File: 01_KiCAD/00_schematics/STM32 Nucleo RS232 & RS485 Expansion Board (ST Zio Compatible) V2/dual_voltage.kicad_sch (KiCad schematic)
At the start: 23 parts, among them IC1 REG103GA-A, U1 TPS2117DRLR

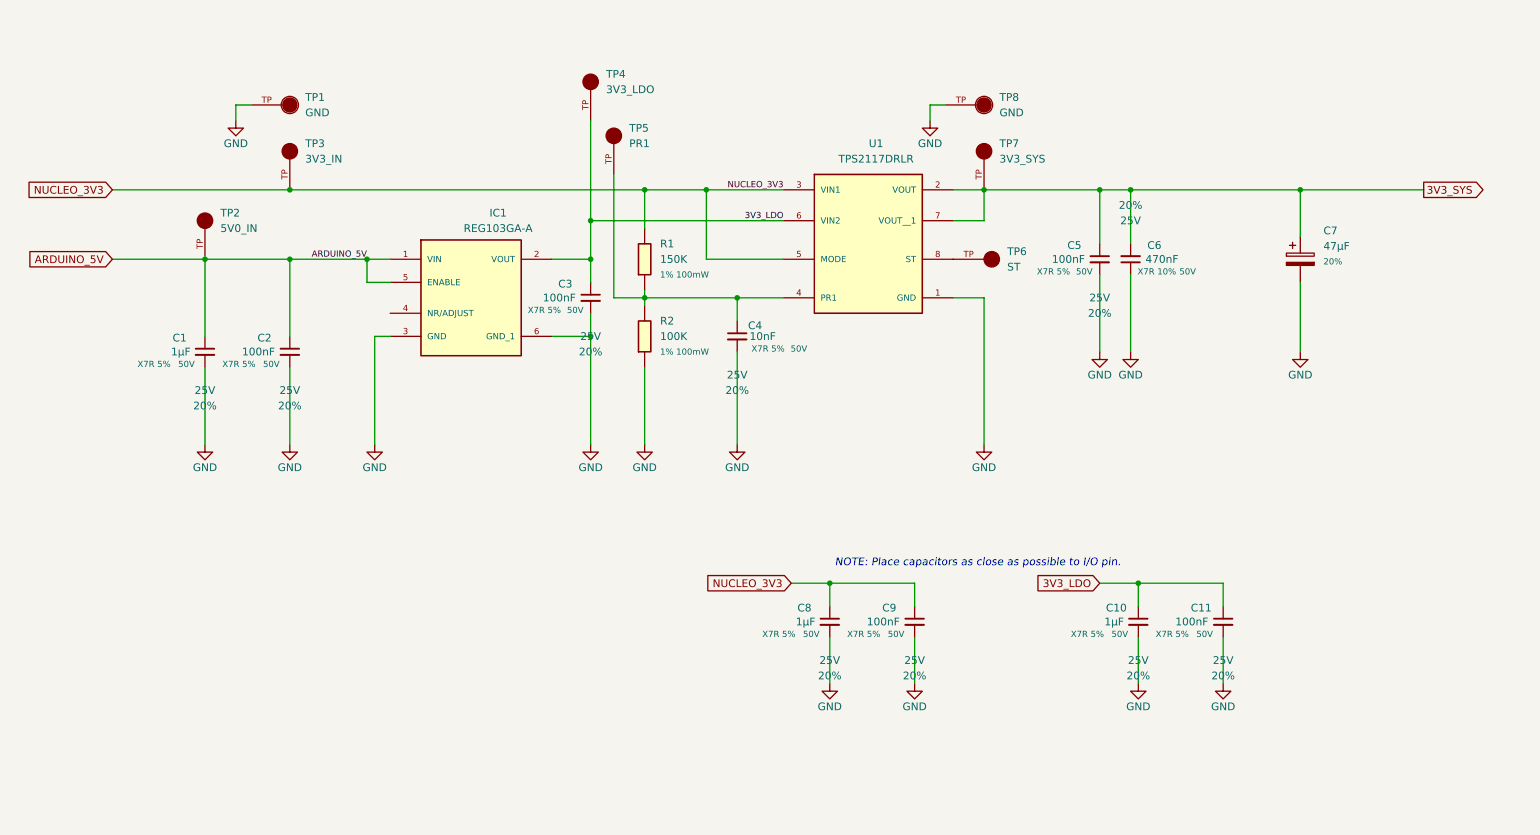
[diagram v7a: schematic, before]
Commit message: Complete redesign
Redesigned the complete board. Added hardware termination jumpers for 1120R resistors for RS485. Changes footprint, package size and simplified values between capacitors.
Still need to re-route the entire board :-(
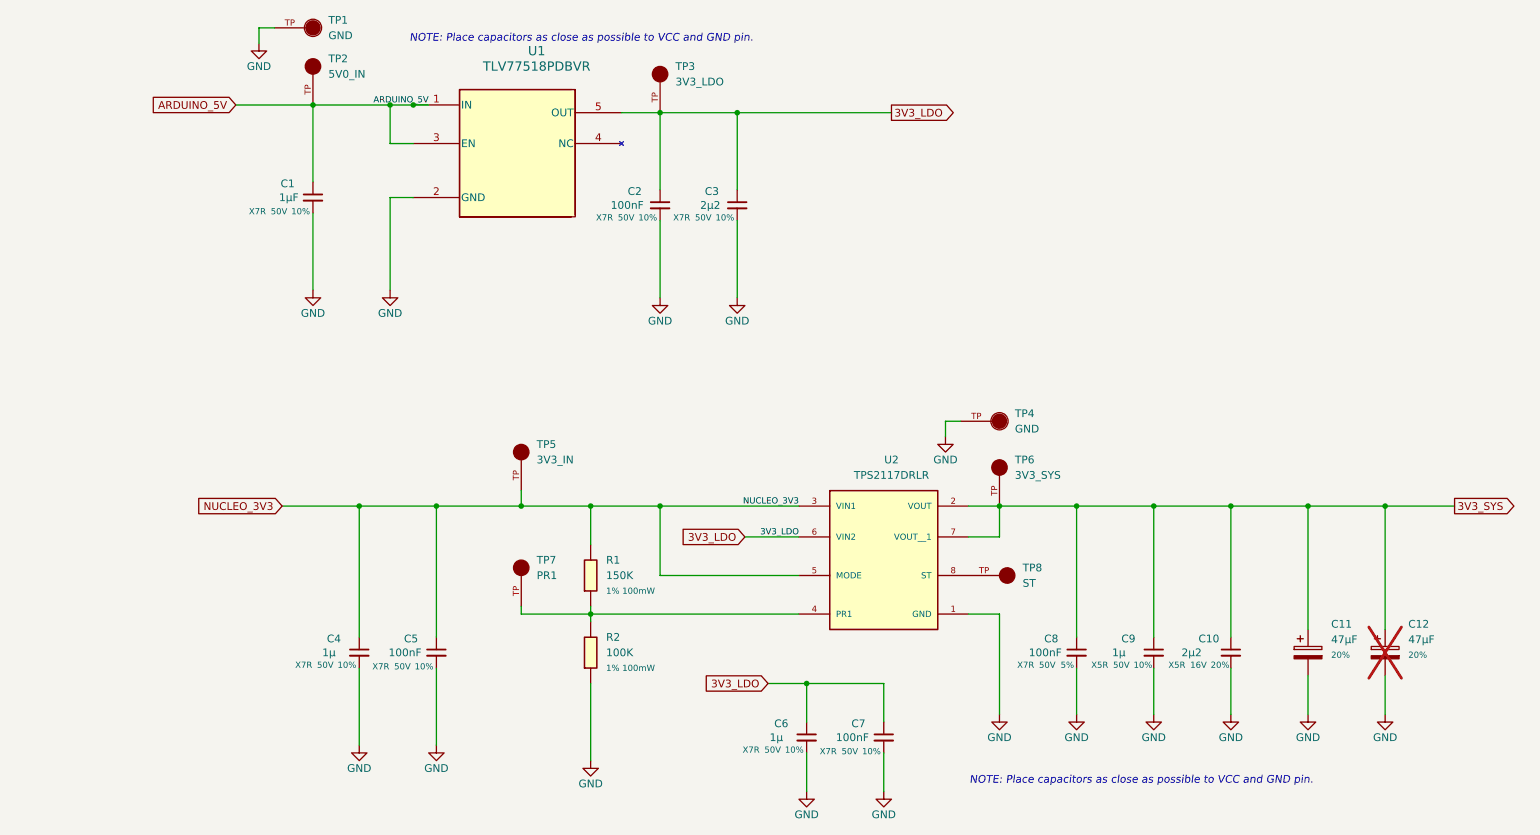
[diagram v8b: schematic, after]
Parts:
- removed C8: 1µF, PCM_SparkFun-Capacitor:C_0603_1608Metric, symbol PCM_SparkFun-Capacitor:0.1uF_0603_25V_20%
- removed C9: 100nF, PCM_SparkFun-Capacitor:C_0603_1608Metric, symbol PCM_SparkFun-Capacitor:0.1uF_0603_25V_20%
- removed IC1: REG103GA-A, REG103GA-A:SOT127P706X180-6N, symbol REG103GA-A:REG103GA-A
- removed TP6: ST, 5007_White:KEYSTONE_5007, symbol 5007_White:5007
- added C10: 2µ2, Capacitor_SMD:C_1210_3225Metric, symbol PCM_SparkFun-Capacitor:0.1uF_0603_25V_20%
- added C12: 47µF, EEEFT1H470AP:CAP_EEEFT1H470AP, symbol Device:C_Polarized
- added C7: 100nF, Capacitor_SMD:C_0805_2012Metric, symbol PCM_SparkFun-Capacitor:0.1uF_0603_25V_20%
- added TP8: ST, 5005_Red:KEYSTONE_5005, symbol 5005_Red:5005
- added U1: TLV77518PDBVR, TLV77518PDBVR:SOT-23-5_1P75X3P05_TEX, symbol TLV77518PDBVR:TLV77518PDBVR
- C1: footprint PCM_SparkFun-Capacitor:C_0603_1608Metric -> Capacitor_SMD:C_0805_2012Metric; Dielectric X7R 5% -> X7R; LCSC C559769 -> C577426; MPN CC0603KRX7R9BB105 -> CS0805KKX7R9BB105; PROD_ID CAP-00810 -> (none); Package 0603 -> 0805; Tolerance 20% -> 10%; Voltage 25V -> 50V
- C2: footprint PCM_SparkFun-Capacitor:C_0603_1608Metric -> Capacitor_SMD:C_0805_2012Metric; Dielectric X7R 5% -> X7R; LCSC C91183 -> C125847; MPN CC0603JRX7R9BB104 -> CC0805KKX7R9BB225; Package 0603 -> 0805; Tolerance 20% -> 10%; Voltage 25V -> 50V
- C3: value 100nF -> 2µ2; footprint PCM_SparkFun-Capacitor:C_0603_1608Metric -> Capacitor_SMD:C_0805_2012Metric; Dielectric X7R 5% -> X7R; LCSC C91183 -> C125847; MPN CC0603JRX7R9BB104 -> CC0805KKX7R9BB225; Package 0603 -> 0805; Tolerance 20% -> 10%; Voltage 25V -> 50V
- C4: value 10nF -> 1µ; footprint PCM_SparkFun-Capacitor:C_0603_1608Metric -> Capacitor_SMD:C_0805_2012Metric; Dielectric X7R 5% -> X7R; LCSC C115056 -> C125847; MPN CC0603JRX7R9BB103 -> CC0805KKX7R9BB225; Package 0603 -> 0805; Tolerance 20% -> 10%; Voltage 25V -> 50V
- C5: footprint PCM_SparkFun-Capacitor:C_0603_1608Metric -> Capacitor_SMD:C_0805_2012Metric; Dielectric X7R 5% -> X7R; LCSC C91183 -> C577426; MPN CC0603JRX7R9BB104 -> CS0805KKX7R9BB105; PROD_ID CAP-00810 -> (none); Package 0603 -> 0805; Tolerance 20% -> 10%; Voltage 25V -> 50V
- C6: value 470nF -> 1µ; footprint PCM_SparkFun-Capacitor:C_0603_1608Metric -> Capacitor_SMD:C_0805_2012Metric; Dielectric X7R 10% -> X7R; LCSC C14663 -> C125847; MPN CC0603KRX7R9BB104 -> CC0805KKX7R9BB225; Package 0603 -> 0805; Tolerance 20% -> 10%; Voltage 25V -> 50V
- C8: renamed from C11; footprint PCM_SparkFun-Capacitor:C_0603_1608Metric -> Capacitor_SMD:C_0603_1608Metric; Dielectric X7R 5% -> X7R; LCSC C91183 -> C24452; MPN CC0603JRX7R9BB104 -> Samsung Electro-Mechanics; Manufacturer YAGEO -> Samsung Electro-Mechanics; PROD_ID CAP-00810 -> (none); Tolerance 20% -> 5%; Voltage 25V -> 50V; Voltage Rating 50V -> (none)
- C9: renamed from C10; value 1µF -> 1µ; footprint PCM_SparkFun-Capacitor:C_0603_1608Metric -> Capacitor_SMD:C_0805_2012Metric; Dielectric X7R 5% -> X5R; LCSC C559769 -> C2932476; MPN CC0603KRX7R9BB105 -> CL21A106KBYQNNE; Manufacturer YAGEO -> Samsung Electro-Mechanics; PROD_ID CAP-00810 -> (none); Package 0603 -> 0805; Tolerance 20% -> 10%; Voltage 25V -> 50V; Voltage Rating 50V -> (none)
- renumbered C7 to C11, TP4 to TP3, TP8 to TP4, TP3 to TP5, TP7 to TP6, TP5 to TP7, U1 to U2
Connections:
- net 3V3_LDO: now also C2.1, C6.1, C7.1, U1.5 (OUT); no longer C8.1, C9.1
- net 3V3_SYS: now also C8.1, C9.1, C10.1, C12.1; no longer C5.1, C6.2
- net ARDUINO_5V: now also U1.1 (IN), U1.3 (EN); no longer C2.1
- net GND: now also C6.2, C10.2, C12.2, C7.2, U1.2 (GND); no longer C6.1
- net NUCLEO_3V3: now also C4.1, C5.1
- net at R1.2, R2.1, TP7.TP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: no longer C4.1
- net at U2.8 (ST): now also TP8.TP
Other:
- note added: "NOTE: Place capacitors as close as possible to VCC and GND pin."
- note removed: "NOTE: Place capacitors as close as possible to I/O pin."
- moved on the sheet: C1, C11, C8, C9, R1, R2, TP1, TP2, TP3, TP4, TP5, TP6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
